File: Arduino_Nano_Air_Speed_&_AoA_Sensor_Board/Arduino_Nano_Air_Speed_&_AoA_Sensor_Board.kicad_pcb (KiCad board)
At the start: 2 copper layers, 99 x 70 mm, 44 parts, among them IC1 MPXV7007DP, J1 Conn_01x04, J2 Conn_01x02_Socket, J3 Conn_01x07_Pin, J4 Conn_01x02_Pin, J5 Conn_01x02_Pin

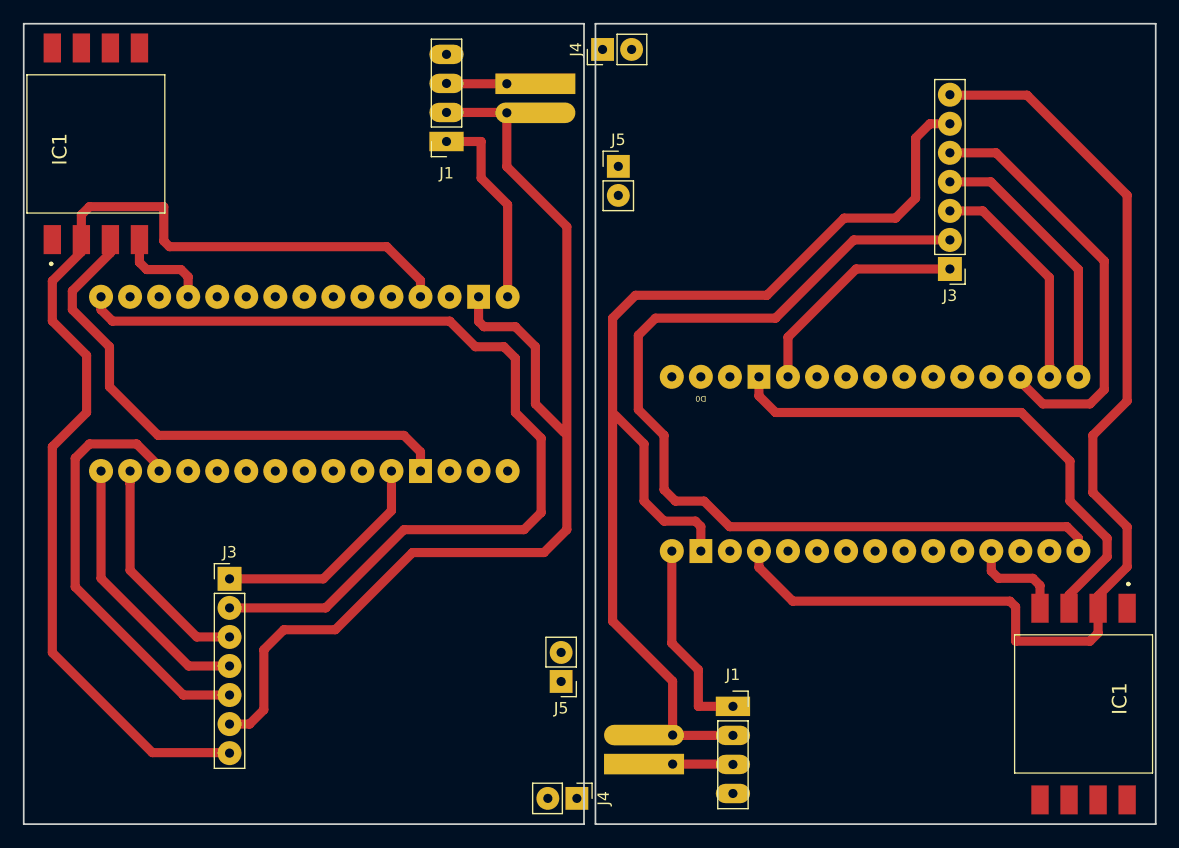
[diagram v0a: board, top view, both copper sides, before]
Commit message: Created a new board for the Wit-Motion WT901B IMU chip.
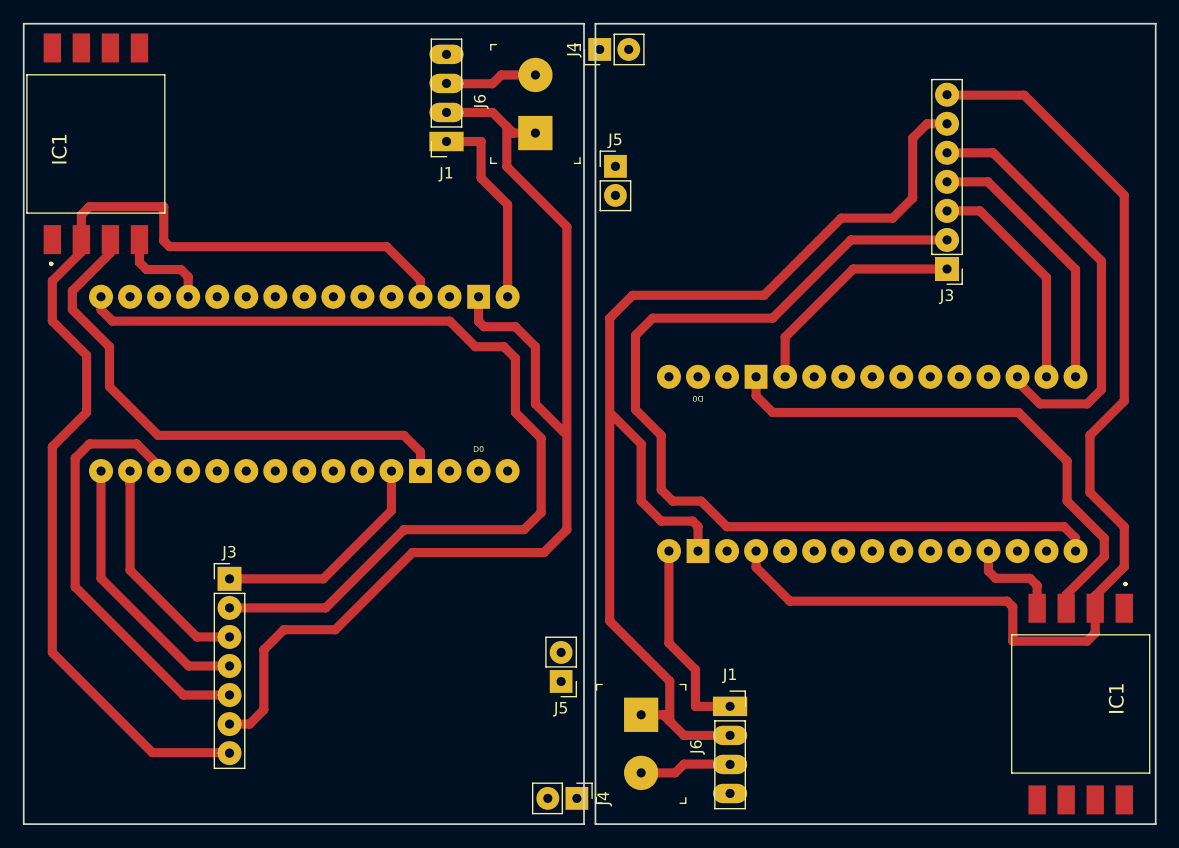
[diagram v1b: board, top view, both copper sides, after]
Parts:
- removed ? (x32): , 
- removed J2: Conn_01x02_Socket, Connector_PinSocket_2.54mm:PinSocket_1x02_P2.54mm_Vertical
- added J6: OSTTC022162, digikey-footprints:Term_Block_1x2_P5.08MM, F.Cu at (93.2, 52.3)
- added J6: OSTTC022162, digikey-footprints:Term_Block_1x2_P5.08MM, F.Cu at (102.5, 103.2)
- added XA1: Arduino_Nano_Socket, Library:Arduino_Nano_Socket, B.Cu at (144.3, 81.2)
- moved XA1 93.4 mm to (51.5, 74.2), turned to 90 degrees
- moved IC1 0.25 mm to (139.8, 102.2)
- moved J1 0.25 mm to (110.3, 102.5)
- moved J3 0.25 mm to (129.2, 64.2)
- moved J4 0.25 mm to (98.9, 45.0)
- moved J5 0.25 mm to (100.2, 55.2)
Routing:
- net +12V: track 12.6 -> 18.7 mm
- net GND: track 200.2 -> 204.8 mm
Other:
- board text added: "6-24V+"
- board text removed: "VCC (6-24V)"
